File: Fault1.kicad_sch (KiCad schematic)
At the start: 15 parts

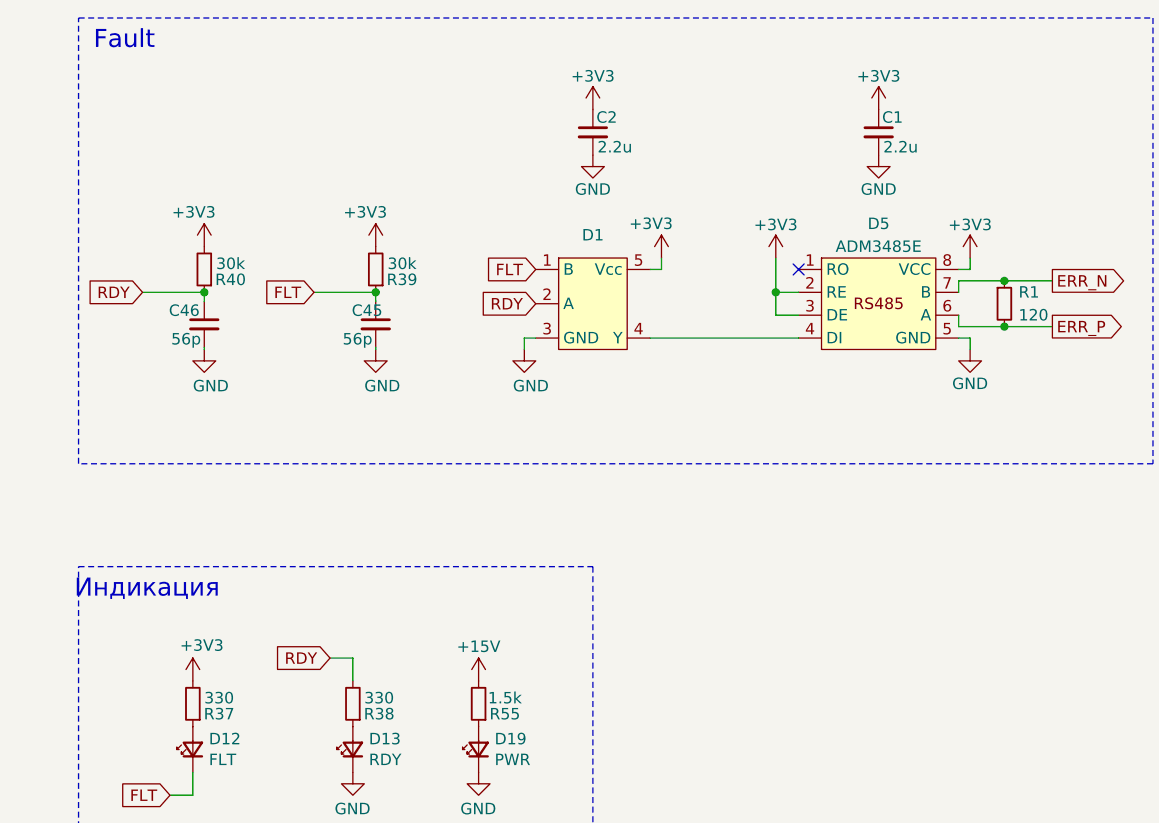
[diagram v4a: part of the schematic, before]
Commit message: Убрал питание 3.3В
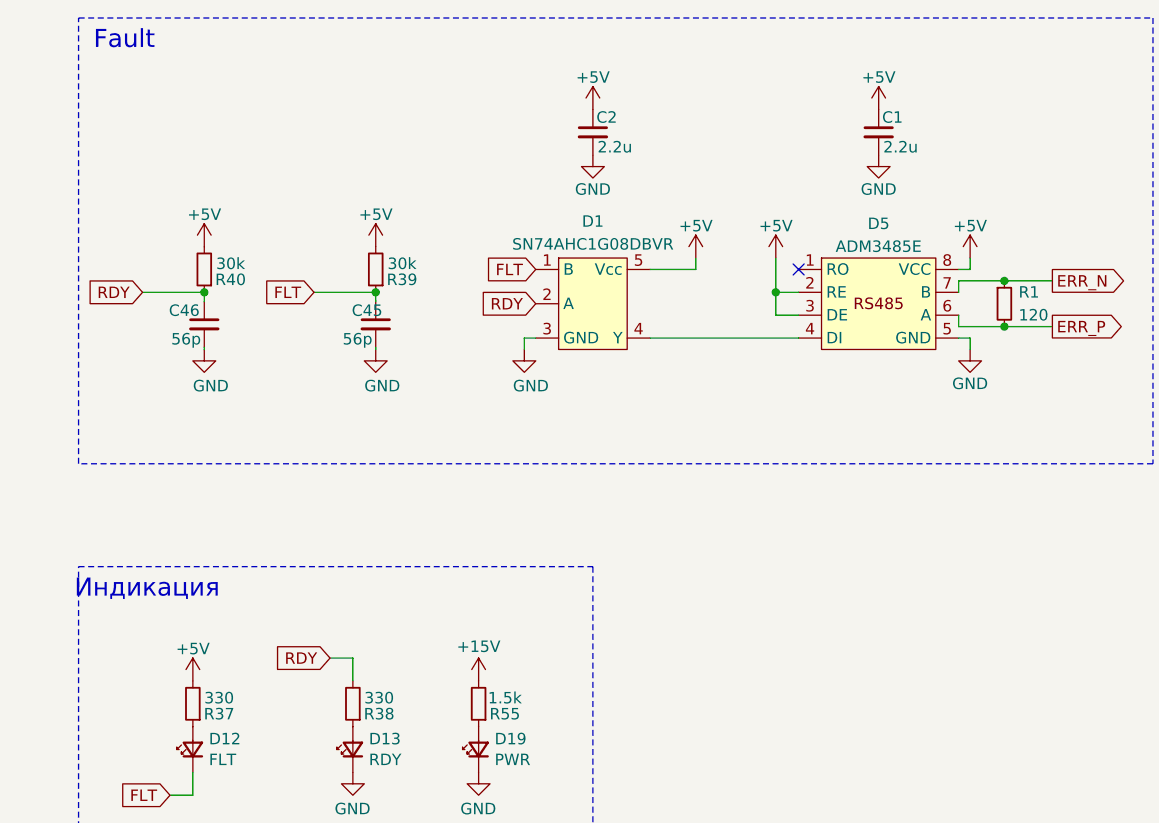
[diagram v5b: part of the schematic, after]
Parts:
- D1: value ~ -> SN74AHC1G08DBVR; footprint (none) -> Package_TO_SOT_SMD:SOT-23-5_HandSoldering
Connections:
- net +3V3 renamed +5V
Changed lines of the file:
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@@
 	(wire
 		(pts
-			(xy 152.4 83.82) (xy 153.67 83.82)
+			(xy 152.4 83.82) (xy 157.48 83.82)
 		)
 		(stroke
@@
 	(wire
 		(pts
-			(xy 153.67 83.82) (xy 153.67 82.55)
+			(xy 157.48 83.82) (xy 157.48 82.55)
 		)
 		(stroke
@@
 	)
 	(symbol
-		(lib_id "power:+3.3V")
+		(lib_id "power:+5V")
 		(at 102.87 81.28 0)
 		(unit 1)
@@
 		(on_board yes)
 		(dnp no)
-		(property "Reference" "#PWR0123"
+		(property "Reference" "#PWR123"
 			(at 102.87 85.09 0)
 			(effects
@@
 			)
 		)
-		(property "Value" "+3V3"
-			(at 104.14 77.47 0)
-			(effects
-				(font
-					(size 1.27 1.27)
-				)
-				(justify right)
+		(property "Value" "+5V"
+			(at 102.87 77.724 0)
+			(effects
+				(font
+					(size 1.27 1.27)
+				)
 			)
 		)
@@
 			)
 		)
-		(property "Description" ""
+		(property "Description" "Power symbol creates a global label with name \"+5V\""
 			(at 102.87 81.28 0)
 			(effects
@@
 			(project "Adapter"
 				(path "/e63e39d7-6ac0-4ffd-8aa3-1841a4541b55/c04386e0-b49e-4fff-b380-675af13a62cb"
-					(reference "#PWR0123")
+					(reference "#PWR123")
 					(unit 1)
 				)
@@
 	)
 	(symbol
-		(lib_id "power:+3.3V")
+		(lib_id "power:+5V")
 		(at 166.37 82.55 0)
 		(unit 1)
@@
 		(on_board yes)
 		(dnp no)
-		(property "Reference" "#PWR05"
+		(property "Reference" "#PWR5"
 			(at 166.37 86.36 0)
 			(effects
@@
 			)
 		)
-		(property "Value" "+3V3"
-			(at 166.37 78.867 0)
+		(property "Value" "+5V"
+			(at 166.37 78.994 0)
 			(effects
 				(font
@@
 			)
 		)
-		(property "Description" ""
+		(property "Description" "Power symbol creates a global label with name \"+5V\""
 			(at 166.37 82.55 0)
 			(effects
@@
 			(project "Adapter"
 				(path "/e63e39d7-6ac0-4ffd-8aa3-1841a4541b55/c04386e0-b49e-4fff-b380-675af13a62cb"
-					(reference "#PWR05")
+					(reference "#PWR5")
 					(unit 1)
 				)
@@
 	)
 	(symbol
-		(lib_id "power:+3.3V")
+		(lib_id "power:+5V")
 		(at 101.6 129.54 0)
 		(unit 1)
@@
 		(on_board yes)
 		(dnp no)
-		(property "Reference" "#PWR0124"
+		(property "Reference" "#PWR124"
 			(at 101.6 133.35 0)
 			(effects
@@
 			)
 		)
-		(property "Value" "+3V3"
-			(at 105.029 125.603 0)
-			(effects
-				(font
-					(size 1.27 1.27)
-				)
-				(justify right)
+		(property "Value" "+5V"
+			(at 101.6 125.984 0)
+			(effects
+				(font
+					(size 1.27 1.27)
+				)
 			)
 		)
@@
 			)
 		)
-		(property "Description" ""
+		(property "Description" "Power symbol creates a global label with name \"+5V\""
 			(at 101.6 129.54 0)
 			(effects
@@
 			(project "Adapter"
 				(path "/e63e39d7-6ac0-4ffd-8aa3-1841a4541b55/c04386e0-b49e-4fff-b380-675af13a62cb"
-					(reference "#PWR0124")
+					(reference "#PWR124")
 					(unit 1)
 				)
@@
 		(on_board yes)
 		(dnp no)
-		(fields_autoplaced yes)
 		(property "Reference" "D1"
-			(at 146.05 80.01 0)
-			(effects
-				(font
-					(size 1.27 1.27)
-				)
-			)
-		)
-		(property "Value" "~"
-			(at 146.05 81.28 0)
-			(effects
-				(font
-					(size 1.27 1.27)
-				)
-			)
-		)
-		(property "Footprint" ""
+			(at 146.05 78.486 0)
+			(effects
+				(font
+					(size 1.27 1.27)
+				)
+			)
+		)
+		(property "Value" "SN74AHC1G08DBVR"
+			(at 146.05 81.026 0)
+			(effects
+				(font
+					(size 1.27 1.27)
+				)
+			)
+		)
+		(property "Footprint" "Package_TO_SOT_SMD:SOT-23-5_HandSoldering"
 			(at 146.05 82.55 0)
 			(effects
@@
 	)
 	(symbol
-		(lib_id "power:+3.3V")
+		(lib_id "power:+5V")
 		(at 146.05 66.04 0)
 		(unit 1)
@@
 		(on_board yes)
 		(dnp no)
-		(property "Reference" "#PWR025"
+		(property "Reference" "#PWR25"
 			(at 146.05 69.85 0)
 			(effects
@@
 			)
 		)
-		(property "Value" "+3V3"
-			(at 146.05 62.357 0)
+		(property "Value" "+5V"
+			(at 146.05 62.484 0)
 			(effects
 				(font
@@
 			)
 		)
-		(property "Description" ""
+		(property "Description" "Power symbol creates a global label with name \"+5V\""
 			(at 146.05 66.04 0)
 			(effects
@@
 			(project "Adapter"
 				(path "/e63e39d7-6ac0-4ffd-8aa3-1841a4541b55/c04386e0-b49e-4fff-b380-675af13a62cb"
-					(reference "#PWR025")
-					(unit 1)
-				)
-			)
-		)
-	)
-	(symbol
-		(lib_id "power:+3.3V")
+					(reference "#PWR25")
+					(unit 1)
+				)
+			)
+		)
+	)
+	(symbol
+		(lib_id "power:+5V")
 		(at 121.92 81.28 0)
 		(unit 1)
@@
 		(on_board yes)
 		(dnp no)
-		(property "Reference" "#PWR0121"
+		(property "Reference" "#PWR121"
 			(at 121.92 85.09 0)
 			(effects
@@
 			)
 		)
-		(property "Value" "+3V3"
-			(at 123.19 77.47 0)
-			(effects
-				(font
-					(size 1.27 1.27)
-				)
-				(justify right)
+		(property "Value" "+5V"
+			(at 121.92 77.724 0)
+			(effects
+				(font
+					(size 1.27 1.27)
+				)
 			)
 		)
@@
 			)
 		)
-		(property "Description" ""
+		(property "Description" "Power symbol creates a global label with name \"+5V\""
 			(at 121.92 81.28 0)
 			(effects
@@
 			(project "Adapter"
 				(path "/e63e39d7-6ac0-4ffd-8aa3-1841a4541b55/c04386e0-b49e-4fff-b380-675af13a62cb"
-					(reference "#PWR0121")
+					(reference "#PWR121")
 					(unit 1)
 				)
@@
 	)
 	(symbol
-		(lib_id "power:+3.3V")
-		(at 153.67 82.55 0)
-		(unit 1)
-		(exclude_from_sim no)
-		(in_bom yes)
-		(on_board yes)
-		(dnp no)
-		(property "Reference" "#PWR01"
-			(at 153.67 86.36 0)
-			(effects
-				(font
-					(size 1.27 1.27)
-				)
-				(hide yes)
-			)
-		)
-		(property "Value" "+3V3"
-			(at 154.94 78.74 0)
-			(effects
-				(font
-					(size 1.27 1.27)
-				)
-				(justify right)
+		(lib_id "power:+5V")
+		(at 157.48 82.55 0)
+		(unit 1)
+		(exclude_from_sim no)
+		(in_bom yes)
+		(on_board yes)
+		(dnp no)
+		(property "Reference" "#PWR1"
+			(at 157.48 86.36 0)
+			(effects
+				(font
+					(size 1.27 1.27)
+				)
+				(hide yes)
+			)
+		)
+		(property "Value" "+5V"
+			(at 157.48 78.994 0)
+			(effects
+				(font
+					(size 1.27 1.27)
+				)
 			)
 		)
 		(property "Footprint" ""
-			(at 153.67 82.55 0)
+			(at 157.48 82.55 0)
 			(effects
 				(font
@@
 		)
 		(property "Datasheet" ""
-			(at 153.67 82.55 0)
-			(effects
-				(font
-					(size 1.27 1.27)
-				)
-				(hide yes)
-			)
-		)
-		(property "Description" ""
-			(at 153.67 82.55 0)
-			(effects
-				(font
-					(size 1.27 1.27)
-				)
-				(hide yes)
-			)
-		)
-		(pin "1"
-		)
-		(instances
-			(project "Adapter"
-				(path "/e63e39d7-6ac0-4ffd-8aa3-1841a4541b55/c04386e0-b49e-4fff-b380-675af13a62cb"
-					(reference "#PWR01")
+			(at 157.48 82.55 0)
+			(effects
+				(font
+					(size 1.27 1.27)
+				)
+				(hide yes)
+			)
+		)
+		(property "Description" "Power symbol creates a global label with name \"+5V\""
+			(at 157.48 82.55 0)
+			(effects
+				(font
+					(size 1.27 1.27)
+				)
+				(hide yes)
+			)
+		)
+		(pin "1"
+		)
+		(instances
+			(project "Adapter"
+				(path "/e63e39d7-6ac0-4ffd-8aa3-1841a4541b55/c04386e0-b49e-4fff-b380-675af13a62cb"
+					(reference "#PWR1")
 					(unit 1)
 				)
@@
 	)
 	(symbol
-		(lib_id "power:+3.3V")
+		(lib_id "power:+5V")
 		(at 177.8 66.04 0)
 		(unit 1)
@@
 		(on_board yes)
 		(dnp no)
-		(property "Reference" "#PWR03"
+		(property "Reference" "#PWR3"
 			(at 177.8 69.85 0)
 			(effects
@@
 			)
 		)
-		(property "Value" "+3V3"
-			(at 177.8 62.357 0)
+		(property "Value" "+5V"
+			(at 177.8 62.484 0)
 			(effects
 				(font
@@
 			)
 		)
-		(property "Description" ""
+		(property "Description" "Power symbol creates a global label with name \"+5V\""
 			(at 177.8 66.04 0)
 			(effects
@@
 			(project "Adapter"
 				(path "/e63e39d7-6ac0-4ffd-8aa3-1841a4541b55/c04386e0-b49e-4fff-b380-675af13a62cb"
-					(reference "#PWR03")
+					(reference "#PWR3")
 					(unit 1)
 				)
@@
 	)
 	(symbol
-		(lib_id "power:+3.3V")
+		(lib_id "power:+5V")
 		(at 187.96 82.55 0)
 		(unit 1)
@@
 		(on_board yes)
 		(dnp no)
-		(property "Reference" "#PWR06"
+		(property "Reference" "#PWR6"
 			(at 187.96 86.36 0)
 			(effects
@@
 			)
 		)
-		(property "Value" "+3V3"
-			(at 187.96 78.867 0)
+		(property "Value" "+5V"
+			(at 187.96 78.994 0)
 			(effects
 				(font
@@
 			)
 		)
-		(property "Description" ""
+		(property "Description" "Power symbol creates a global label with name \"+5V\""
 			(at 187.96 82.55 0)
 			(effects
@@
 			(project "Adapter"
 				(path "/e63e39d7-6ac0-4ffd-8aa3-1841a4541b55/c04386e0-b49e-4fff-b380-675af13a62cb"
-					(reference "#PWR06")
-					(unit 1)
-				)
+					(reference "#PWR6")
+					(unit 1)
+				)

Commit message: Развел вторую стойку
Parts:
- added C82, C83, C86, C87: 56p, Capacitor_SMD:C_0805_2012Metric_Pad1.18x1.45mm_HandSolder, symbol Device:C_Small
- added C84, C85, C88, C89: 2.2u, Capacitor_SMD:C_0805_2012Metric_Pad1.18x1.45mm_HandSolder, symbol Device:C_Small
- added D23, D25: SN74AHC1G08DBVR, Package_TO_SOT_SMD:SOT-23-5_HandSoldering, symbol Logic_My:MC74VHC1GT08DTT1G
- added D24, D26: ADM3485E, Package_SO:SOIC-8_3.9x4.9mm_P1.27mm, symbol Interface_My:ADM3485E_1
- added D27, D30: FLT, LED_SMD:LED_0805_2012Metric_Pad1.15x1.40mm_HandSolder, symbol Device:LED_Small
- added D28, D49: RDY, LED_SMD:LED_0805_2012Metric_Pad1.15x1.40mm_HandSolder, symbol Device:LED_Small
- added D29, D50: PWR, LED_SMD:LED_0805_2012Metric_Pad1.15x1.40mm_HandSolder, symbol Device:LED_Small
- added R75, R76, R78, R82: 30k, Resistor_SMD:R_0805_2012Metric_Pad1.20x1.40mm_HandSolder, symbol Device:R_Small
- added R77, R84: 120, Resistor_SMD:R_0805_2012Metric_Pad1.20x1.40mm_HandSolder, symbol Device:R_Small
- added R87, R88, R90, R94: 330, Resistor_SMD:R_0805_2012Metric_Pad1.20x1.40mm_HandSolder, symbol Device:R_Small
- added R89, R96: 1.5k, Resistor_SMD:R_0805_2012Metric_Pad1.20x1.40mm_HandSolder, symbol Device:R_Small
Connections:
- net +15V: now also R89.2, R96.2
- net +5V: now also C84.1, C85.1, C88.1, C89.1, D23.5 (Vcc), D24.2 (RE), D24.3 (DE), D24.8 (VCC), D25.5 (Vcc), D26.2 (RE), D26.3 (DE), D26.8 (VCC), R75.2, R76.2, R78.2, R82.2, R87.2, R90.2
- net GND: now also C82.2, C83.2, C84.2, C85.2, C86.2, C87.2, C88.2, C89.2, D23.3 (GND), D24.5 (GND), D25.3 (GND), D26.5 (GND), D28.1 (K), D29.1 (K), D49.1 (K), D50.1 (K)
- net ERR_N renamed ERR_A_N
- net ERR_P renamed ERR_A_P
- net FLT renamed FLT_A
- net RDY renamed RDY_A
- new net: D30.2 (A), R90.1
- new net: D49.2 (A), R94.1
- new net: D25.4 (Y), D26.4 (DI)
- new net: D50.2 (A), R96.1
- new net: D29.2 (A), R89.1
- new net: D28.2 (A), R88.1
- new net: D27.2 (A), R87.1
- new net: D23.4 (Y), D24.4 (DI)
- new net ERR_B_N: D24.7 (B), R77.1
- new net ERR_B_P: D24.6 (A), R77.2
- new net ERR_C_N: D26.7 (B), R84.1
- new net ERR_C_P: D26.6 (A), R84.2
- new net FLT_B: C83.1, D23.1 (B), D27.1 (K), R76.1
- new net FLT_C: C87.1, D25.1 (B), D30.1 (K), R82.1
- new net RDY_B: C82.1, D23.2 (A), R75.1, R88.2
- new net RDY_C: C86.1, D25.2 (A), R78.1, R94.2
- no-connect marks 1 -> 3
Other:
- note added: "Fault A"
- note added: "Fault B"
- note added: "Fault C"
- note added: "Индикация A"
- note added: "Индикация B"
- note added: "Индикация C"
- note removed: "Fault"
- note removed: "Индикация"
- moved on the sheet: C1, C2, C45, C46, D1, D12, D13, D19, D5, R1, R37, R38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
